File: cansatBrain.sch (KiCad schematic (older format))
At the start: 33 parts

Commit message: everything
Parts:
- removed BT?: BATTERY, symbol BATTERY
- removed C? (x3): 10 uF, symbol C
- removed C?: 0.1 uF, symbol C
- removed D?: DIODE, symbol DIODE
- removed L?: 1.5 uH, symbol INDUCTOR
- removed Q?: MOS_P, symbol MOS_P
- removed R? (x4): R, symbol R
- removed SW?: SW_PUSH_4, symbol SW_PUSH_4
- removed U?: TMP102, symbol TMP102
- removed U?: TPS63031, symbol TPS63031
- added C? (x4): 100nF, symbol C
- added C? (x4): 10uF, symbol CP2
- added C? (x3): 1uF, symbol C
- added C?: 10nF, symbol C
- added C?: 0.1uF, symbol C
- added C?: 10uF, symbol C
- added P?: Ext_Temp, symbol CONN_01X04
- added SW?: SW_PUSH_4, symbol SW_PUSH_4
- R? (x5): value R -> 1K
- R? (x2): value R -> 1M
- R? (x2): value R -> 100
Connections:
- net labels added: BAT_SENSE, BUTTON, GNDA, MPU_INT, SD_CS, VCCA, XBEE_SLEEP, XTRA_RX, XTRA_TX
- net labels removed: VBAT, VIN
- wire segments 115 -> 116
- no-connect marks 1 -> 31
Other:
- note removed: "1/3N lithium cell"
- moved on the sheet: P?, Q?, R?, U?

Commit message: ran rescue
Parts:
- C? (x10): symbol C -> C-RESCUE-cansatBrain
- R? (x9): symbol R -> R-RESCUE-cansatBrain
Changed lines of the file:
@@
 EESchema Schematic File Version 2
+LIBS:cansatBrain-rescue
 LIBS:power
 LIBS:device
@@
 $EndDescr
 $Comp
-L GND #PWR?
+L GND-RESCUE-cansatBrain #PWR?
 U 1 1 55860B07
 P 850 7500
@@
 SCL
 $Comp
-L R R?
+L R-RESCUE-cansatBrain R?
 U 1 1 5593D5CF
 P 2800 4450
@@
 $EndComp
 $Comp
-L R R?
+L R-RESCUE-cansatBrain R?
 U 1 1 5593D624
 P 2800 4650
@@
 XBEE_TX
 $Comp
-L R R?
+L R-RESCUE-cansatBrain R?
 U 1 1 5593EE71
 P 2750 4150
@@
 $EndComp
 $Comp
-L R R?
+L R-RESCUE-cansatBrain R?
 U 1 1 5593EE77
 P 3100 4250
@@
 	7950 3450 7950 3350
 $Comp
-L GND #PWR?
+L GND-RESCUE-cansatBrain #PWR?
 U 1 1 55947E65
 P 7550 3450
@@
 	7550 3350 7950 3350
 $Comp
-L GND #PWR?
+L GND-RESCUE-cansatBrain #PWR?
 U 1 1 55948C97
 P 5350 7300
@@
 	2450 1200 2450 1250
 $Comp
-L GND #PWR?
+L GND-RESCUE-cansatBrain #PWR?
 U 1 1 5594DF95
 P 2450 1250
@@
 	2300 1100 2900 1100
 $Comp
-L R R?
+L R-RESCUE-cansatBrain R?
 U 1 1 55950062
 P 2350 1650
@@
 $EndComp
 $Comp
-L R R?
+L R-RESCUE-cansatBrain R?
 U 1 1 55951A1D
 P 2650 1000
@@
 Connection ~ 2100 1550
 $Comp
-L R R?
+L R-RESCUE-cansatBrain R?
 U 1 1 5595265B
 P 1650 1550
@@
 Connection ~ 7500 950
 $Comp
-L GND #PWR?
+L GND-RESCUE-cansatBrain #PWR?
 U 1 1 5595A08F
 P 7500 1250
@@
 $EndComp
 $Comp
-L R R?
+L R-RESCUE-cansatBrain R?
 U 1 1 55962027
 P 4550 6050
@@
 SCL
 $Comp
-L R R?
+L R-RESCUE-cansatBrain R?
 U 1 1 55967163
 P 4800 5750
@@
 $EndComp
 $Comp
-L GNDA #PWR?
+L GNDA-RESCUE-cansatBrain #PWR?
 U 1 1 55947C02
 P 5150 3950
@@
 $EndComp
 $Comp
-L GNDA #PWR?
+L GNDA-RESCUE-cansatBrain #PWR?
 U 1 1 5594830F
 P 6000 2200
@@
 $EndSheet
 $Comp
-L C C?
+L C-RESCUE-cansatBrain C?
 U 1 1 5595C2F2
 P 6150 3300
@@
 $EndComp
 $Comp
-L C C?
+L C-RESCUE-cansatBrain C?
 U 1 1 5595C2FE
 P 6400 3300
@@
 $EndComp
 $Comp
-L GNDA #PWR?
+L GNDA-RESCUE-cansatBrain #PWR?
 U 1 1 5595C306
 P 6650 3500
@@
 $EndComp
 $Comp
-L GNDA #PWR?
+L GNDA-RESCUE-cansatBrain #PWR?
 U 1 1 5595C30C
 P 6400 3500
@@
 $EndComp
 $Comp
-L GNDA #PWR?
+L GNDA-RESCUE-cansatBrain #PWR?
 U 1 1 5595C312
 P 6150 3500
@@
 Connection ~ 6150 3050
 $Comp
-L C C?
+L C-RESCUE-cansatBrain C?
 U 1 1 5595DCAA
 P 5850 3800
@@
 	5850 3600 5600 3600
 $Comp
-L GNDA #PWR?
+L GNDA-RESCUE-cansatBrain #PWR?
 U 1 1 5595E48A
 P 5850 4050
@@
 $EndComp
 $Comp
-L GNDA #PWR?
+L GNDA-RESCUE-cansatBrain #PWR?
 U 1 1 5594C5A2
 P 4450 5000
@@
 BAT_SENSE
 $Comp
-L GNDA #PWR?
+L GNDA-RESCUE-cansatBrain #PWR?
 U 1 1 5595C817
 P 4600 1550
@@
 	5350 6300 6100 6300
 $Comp
-L C C?
+L C-RESCUE-cansatBrain C?
 U 1 1 559679F4
 P 5600 6550
@@
 $EndComp
 $Comp
-L C C?
+L C-RESCUE-cansatBrain C?
 U 1 1 55967A00
 P 5850 6550
@@
 Connection ~ 5350 6300
 $Comp
-L GND #PWR?
+L GND-RESCUE-cansatBrain #PWR?
 U 1 1 55967EFF
 P 5600 6750
@@
 $EndComp
 $Comp
-L GND #PWR?
+L GND-RESCUE-cansatBrain #PWR?
 U 1 1 55967F36
 P 5850 6750
@@
 $EndComp
 $Comp
-L GND #PWR?
+L GND-RESCUE-cansatBrain #PWR?
 U 1 1 55967F6D
 P 6100 6750
@@
 $EndComp
 $Comp
-L C C?
+L C-RESCUE-cansatBrain C?
 U 1 1 5596DE7F
 P 4650 2400
@@
 $EndComp
 $Comp
-L GNDA #PWR?
+L GNDA-RESCUE-cansatBrain #PWR?
 U 1 1 5596E206
 P 4650 2600
@@
 	3600 1800 3600 1900
 $Comp
-L C C?
+L C-RESCUE-cansatBrain C?
 U 1 1 5596F8E8
 P 3600 2100
@@
 $EndComp
 $Comp
-L GNDA #PWR?
+L GNDA-RESCUE-cansatBrain #PWR?
 U 1 1 5596F93A
 P 3600 2300
@@
 NoConn ~ 5950 1800
 $Comp
-L GNDA #PWR?
+L GNDA-RESCUE-cansatBrain #PWR?
 U 1 1 5597096F
 P 6000 1950
@@
 NoConn ~ 5950 1400
 $Comp
-L GNDA #PWR?
+L GNDA-RESCUE-cansatBrain #PWR?
 U 1 1 55970FAD
 P 4300 1150
@@
 	4300 1100 4750 1100
 $Comp
-L C C?
+L C-RESCUE-cansatBrain C?
 U 1 1 5597608A
 P 3850 2350
@@
 $EndComp
 $Comp
-L C C?
+L C-RESCUE-cansatBrain C?
 U 1 1 55976096
 P 4100 2350
@@
 $EndComp
 $Comp
-L GNDA #PWR?
+L GNDA-RESCUE-cansatBrain #PWR?
 U 1 1 5597609C
 P 4350 2550
@@
 $EndComp
 $Comp
-L GNDA #PWR?
+L GNDA-RESCUE-cansatBrain #PWR?
 U 1 1 559760A2
 P 4100 2550
@@
 $EndComp
 $Comp
-L GNDA #PWR?
+L GNDA-RESCUE-cansatBrain #PWR?
 U 1 1 559760A8
 P 3850 2550
@@
 NoConn ~ 7700 1400
 $Comp
-L C C?
+L C-RESCUE-cansatBrain C?
 U 1 1 5598A4C3
 P 700 4250
@@
 $EndComp
 $Comp
-L GND #PWR?
+L GND-RESCUE-cansatBrain #PWR?
 U 1 1 5598A51D
 P 700 4450
@@
 Connection ~ 900  4050
 $Comp
-L GND #PWR?
+L GND-RESCUE-cansatBrain #PWR?
 U 1 1 5598DC65
 P 6850 1350
@@
 	7450 4600 7450 4750
 $Comp
-L GND #PWR?
+L GND-RESCUE-cansatBrain #PWR?
 U 1 1 559A8264
 P 7450 4750

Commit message: worked on stuff
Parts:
- P?: value Ext_Temp -> I2C

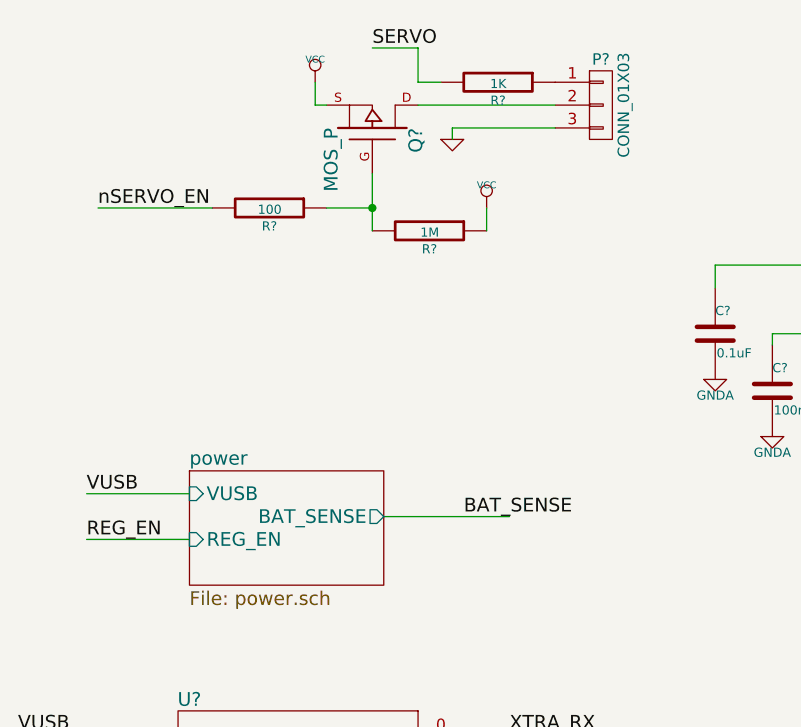
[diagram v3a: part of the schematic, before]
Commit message: changed button voltage clamp
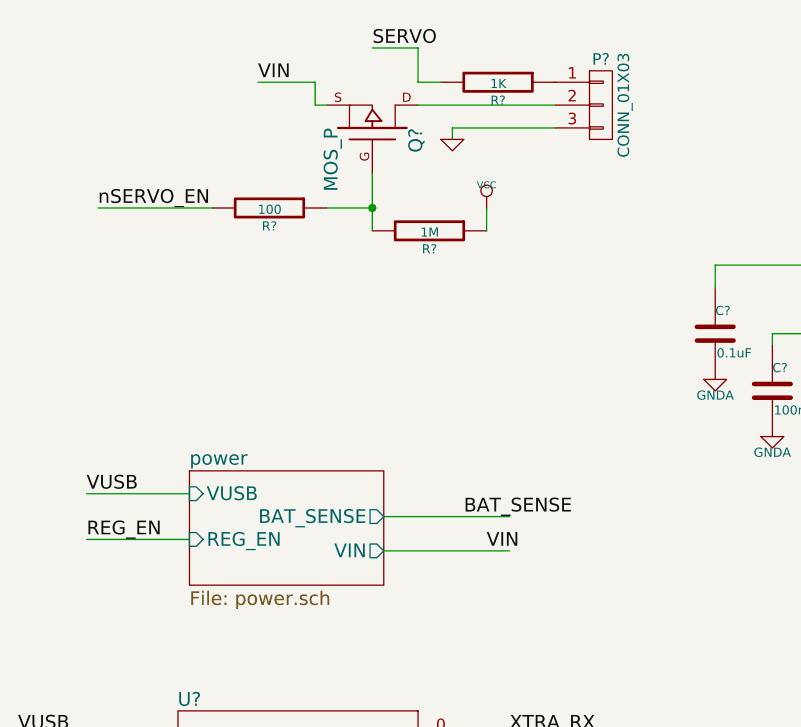
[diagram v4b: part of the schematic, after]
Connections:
- net labels added: VIN
- wire segments 116 -> 118
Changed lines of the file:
@@
-	1    0    0    -1
-$EndComp
-$Comp
-L VCC #PWR06
-U 1 1 5594DE9A
-P 1850 1000
-F 0 "#PWR06" H 1850 1100 30  0001 C CNN
-F 1 "VCC" H 1850 1100 30  0000 C CNN
-F 2 "" H 1850 1000 60  0000 C CNN
-F 3 "" H 1850 1000 60  0000 C CNN
-	1    1850 1000
 	1    0    0    -1
 $EndComp
@@
 F3 "REG_EN" I L 1300 3000 60
 F4 "BAT_SENSE" O R 2150 2900 60
+F5 "VIN" O R 2150 3050 60
 $EndSheet
 $Comp
@@
 NoConn ~ 2500 5350
 NoConn ~ 2500 5450
+Wire Wire Line
+	2150 3050 2700 3050
+Text Label 2600 3050 0    60   ~ 0
+VIN
+Wire Wire Line
+	1850 1000 1600 1000
+Text Label 1600 1000 0    60   ~ 0
+VIN
 $EndSCHEMATC

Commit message: did more work
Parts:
- removed SW?: SW_PUSH_4, symbol SW_PUSH_4
- added P?: CONN_01X03, symbol CONN_01X03
- added Q?: MOS_P, symbol MOS_P
- added R?: 1M, symbol R-RESCUE-cansatBrain
- added R?: 100, symbol R-RESCUE-cansatBrain
- added R? (x2): 10k, symbol R
- added U?: ArduCAM-M-2MP, symbol ArduCAM-M-2MP
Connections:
- net labels added: +5V, CAM_CS, PITOT_TUBE, nPITOT_EN
- wire segments 118 -> 140
- no-connect marks 31 -> 28

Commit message: more stuff
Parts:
- added P4: CONN_01X04, symbol CONN_01X04
- gave numbers to parts that had none: 40
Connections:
- net M0SI is gone; now on net MOSI: U1.11 (11(DOUT))
- net GND: now also P4.4 (P4)
- net VCC: now also P4.3 (P3)
- net VCCA: now also C6.1
- net XTRA_RX: now also P4.2 (P2)
- net XTRA_TX: now also P4.1 (P1)

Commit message: footprints
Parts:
- C1, C10, C11, C12, C13, C14, C2, C3, C4, C5, C6, C7, C8, C9: footprint (none) -> Capacitors_SMD:C_0402
- P1, P3: footprint (none) -> Pin_Headers:Pin_Header_Straight_1x03
- P2, P4: footprint (none) -> Pin_Headers:Pin_Header_Straight_1x04
- Q1, Q2, Q3: footprint (none) -> TO_SOT_Packages_SMD:SOT-23_Handsoldering
- R1, R10, R11, R12, R13, R2, R3, R4, R5, R6, R7, R8, R9: footprint (none) -> Resistors_SMD:R_0402
- U1: footprint (none) -> Housings_DIP:DIP-28_W15.24mm
- U2: footprint (none) -> SMD_Packages:SOIC-8-N
- U3: footprint (none) -> Pin_Headers:Pin_Header_Straight_1x06
- U4: footprint (none) -> Housings_DFN_QFN:QFN-24-1EP_3x3mm_Pitch0.4mm
- U5: footprint (none) -> Pin_Headers:Pin_Header_Straight_1x05
- U6: footprint (none) -> Housings_DIP:DIP-20_W7.62mm_LongPads
- U7: footprint (none) -> Pin_Headers:Pin_Header_Straight_1x08
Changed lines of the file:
@@
 F 0 "U4" H 5350 2350 60  0000 C CNN
 F 1 "MPU-9250" H 5350 950 60  0000 C CNN
-F 2 "" H 5450 1750 60  0000 C CNN
+F 2 "Housings_DFN_QFN:QFN-24-1EP_3x3mm_Pitch0.4mm" H 5450 1750 60  0001 C CNN
 F 3 "" H 5450 1750 60  0000 C CNN
 	1    5350 1650
@@
 F 0 "U6" H 7950 2400 60  0000 C CNN
 F 1 "XBee" H 8000 800 60  0000 C CNN
-F 2 "" H 9350 1050 60  0000 C CNN
+F 2 "Housings_DIP:DIP-20_W7.62mm_LongPads" H 9350 1050 60  0001 C CNN
 F 3 "" H 9350 1050 60  0000 C CNN
 	1    8650 1600
@@
 F 0 "U2" H 4800 3100 60  0000 L CNN
 F 1 "MPL3115A2" H 5200 3100 60  0000 L CNN
-F 2 "" H 6400 1700 60  0000 C CNN
+F 2 "SMD_Packages:SOIC-8-N" H 6400 1700 60  0001 C CNN
 F 3 "" H 6400 1700 60  0000 C CNN
 	1    5150 3450
@@
 F 0 "U3" H 5000 7100 60  0000 C CNN
 F 1 "microSD" H 5050 6500 60  0000 C CNN
-F 2 "" H 4950 6750 60  0000 C CNN
+F 2 "Pin_Headers:Pin_Header_Straight_1x06" H 4950 6750 60  0001 C CNN
 F 3 "" H 4950 6750 60  0000 C CNN
 	1    5250 6800
@@
 F 0 "U5" H 8200 3900 60  0000 C CNN
 F 1 "LS20031" H 8350 3100 60  0000 C CNN
-F 2 "" H 7900 3550 60  0000 C CNN
+F 2 "Pin_Headers:Pin_Header_Straight_1x05" H 7900 3550 60  0001 C CNN
 F 3 "" H 7900 3550 60  0000 C CNN
 	1    8250 3500
@@
 F 0 "U1" H 1300 6900 60  0000 C CNN
 F 1 "Teensy_LC" H 1450 3050 60  0000 C CNN
-F 2 "" H 1650 5900 60  0000 C CNN
+F 2 "Housings_DIP:DIP-28_W15.24mm" H 1650 5900 60  0001 C CNN
 F 3 "" H 1650 5900 60  0000 C CNN
 	1    1800 5300
@@
 F 0 "R5" V 2880 4450 40  0000 C CNN
 F 1 "1K" V 2807 4451 40  0000 C CNN
-F 2 "" V 2730 4450 30  0000 C CNN
+F 2 "Resistors_SMD:R_0402" V 2730 4450 30  0001 C CNN
 F 3 "" H 2800 4450 30  0000 C CNN
 	1    2800 4450
@@
 F 0 "R6" V 2880 4650 40  0000 C CNN
 F 1 "1K" V 2807 4651 40  0000 C CNN
-F 2 "" V 2730 4650 30  0000 C CNN
+F 2 "Resistors_SMD:R_0402" V 2730 4650 30  0001 C CNN
 F 3 "" H 2800 4650 30  0000 C CNN
 	1    2800 4650
@@
 F 0 "R4" V 2830 4150 40  0000 C CNN
 F 1 "1K" V 2757 4151 40  0000 C CNN
-F 2 "" V 2680 4150 30  0000 C CNN
+F 2 "Resistors_SMD:R_0402" V 2680 4150 30  0001 C CNN
 F 3 "" H 2750 4150 30  0000 C CNN
 	1    2750 4150
@@
 F 0 "R7" V 3180 4250 40  0000 C CNN
 F 1 "1K" V 3107 4251 40  0000 C CNN
-F 2 "" V 3030 4250 30  0000 C CNN
+F 2 "Resistors_SMD:R_0402" V 3030 4250 30  0001 C CNN
 F 3 "" H 3100 4250 30  0000 C CNN
 	1    3100 4250
@@
 F 0 "P1" H 3100 1300 50  0000 C CNN
 F 1 "CONN_01X03" V 3200 1100 50  0000 C CNN
-F 2 "" H 3100 1100 60  0000 C CNN
+F 2 "Pin_Headers:Pin_Header_Straight_1x03" H 3100 1100 60  0001 C CNN
 F 3 "" H 3100 1100 60  0000 C CNN
 	1    3100 1100
@@
 F 0 "Q1" H 2100 1390 60  0000 R CNN
 F 1 "MOS_P" H 2100 1020 60  0000 R CNN
-F 2 "" H 2100 1200 60  0000 C CNN
+F 2 "TO_SOT_Packages_SMD:SOT-23_Handsoldering" H 2100 1200 60  0001 C CNN
 F 3 "" H 2100 1200 60  0000 C CNN
 	1    2100 1200
@@
 F 0 "R2" V 2430 1650 40  0000 C CNN
 F 1 "1M" V 2357 1651 40  0000 C CNN
-F 2 "" V 2280 1650 30  0000 C CNN
+F 2 "Resistors_SMD:R_0402" V 2280 1650 30  0001 C CNN
 F 3 "" H 2350 1650 30  0000 C CNN
 	1    2350 1650
@@
 F 0 "R3" V 2730 1000 40  0000 C CNN
 F 1 "1K" V 2657 1001 40  0000 C CNN
-F 2 "" V 2580 1000 30  0000 C CNN
+F 2 "Resistors_SMD:R_0402" V 2580 1000 30  0001 C CNN
 F 3 "" H 2650 1000 30  0000 C CNN
 	1    2650 1000
@@
 F 0 "R1" V 1730 1550 40  0000 C CNN
 F 1 "100" V 1657 1551 40  0000 C CNN
-F 2 "" V 1580 1550 30  0000 C CNN
+F 2 "Resistors_SMD:R_0402" V 1580 1550 30  0001 C CNN
 F 3 "" H 1650 1550 30  0000 C CNN
 	1    1650 1550
@@
 F 0 "Q2" H 5250 6240 60  0000 R CNN
 F 1 "MOS_P" H 5250 5870 60  0000 R CNN
-F 2 "" H 5250 6050 60  0000 C CNN
+F 2 "TO_SOT_Packages_SMD:SOT-23_Handsoldering" H 5250 6050 60  0001 C CNN
 F 3 "" H 5250 6050 60  0000 C CNN
 	1    5250 6050
@@
 F 0 "R8" V 4630 6050 40  0000 C CNN
 F 1 "100" V 4557 6051 40  0000 C CNN
-F 2 "" V 4480 6050 30  0000 C CNN
+F 2 "Resistors_SMD:R_0402" V 4480 6050 30  0001 C CNN
 F 3 "" H 4550 6050 30  0000 C CNN
 	1    4550 6050
@@
 F 0 "R9" V 4880 5750 40  0000 C CNN
 F 1 "1M" V 4807 5751 40  0000 C CNN
-F 2 "" V 4730 5750 30  0000 C CNN
+F 2 "Resistors_SMD:R_0402" V 4730 5750 30  0001 C CNN
 F 3 "" H 4800 5750 30  0000 C CNN
 	1    4800 5750
@@
 F 0 "C11" H 6150 3400 40  0000 L CNN
 F 1 "100nF" H 6156 3215 40  0000 L CNN
-F 2 "" H 6188 3150 30  0000 C CNN
+F 2 "Capacitors_SMD:C_0402" H 6188 3150 30  0001 C CNN
 F 3 "" H 6150 3300 60  0000 C CNN
 	1    6150 3300
@@
 F 0 "C13" H 6650 3400 40  0000 L CNN
 F 1 "10uF" H 6656 3215 40  0000 L CNN
-F 2 "" H 6688 3150 30  0000 C CNN
+F 2 "Capacitors_SMD:C_0402" H 6688 3150 30  0001 C CNN
 F 3 "" H 6650 3300 60  0000 C CNN
 	1    6650 3300
@@
 F 0 "C12" H 6400 3400 40  0000 L CNN
 F 1 "1uF" H 6406 3215 40  0000 L CNN
-F 2 "" H 6438 3150 30  0000 C CNN
+F 2 "Capacitors_SMD:C_0402" H 6438 3150 30  0001 C CNN
 F 3 "" H 6400 3300 60  0000 C CNN
 	1    6400 3300
@@
 F 0 "C8" H 5850 3900 40  0000 L CNN
 F 1 "100nF" H 5856 3715 40  0000 L CNN
-F 2 "" H 5888 3650 30  0000 C CNN
+F 2 "Capacitors_SMD:C_0402" H 5888 3650 30  0001 C CNN
 F 3 "" H 5850 3800 60  0000 C CNN
 	1    5850 3800
@@
 F 0 "P2" H 5500 5200 50  0000 C CNN
 F 1 "I2C" V 5600 4950 50  0000 C CNN
-F 2 "" H 5500 4950 60  0000 C CNN
+F 2 "Pin_Headers:Pin_Header_Straight_1x04" H 5500 4950 60  0001 C CNN
 F 3 "" H 5500 4950 60  0000 C CNN
 	1    5500 4950
@@
 F 0 "C7" H 5600 6650 40  0000 L CNN
 F 1 "100nF" H 5606 6465 40  0000 L CNN
-F 2 "" H 5638 6400 30  0000 C CNN
+F 2 "Capacitors_SMD:C_0402" H 5638 6400 30  0001 C CNN
 F 3 "" H 5600 6550 60  0000 C CNN
 	1    5600 6550
@@
 F 0 "C10" H 6100 6650 40  0000 L CNN
 F 1 "10uF" H 6106 6465 40  0000 L CNN
-F 2 "" H 6138 6400 30  0000 C CNN
+F 2 "Capacitors_SMD:C_0402" H 6138 6400 30  0001 C CNN
 F 3 "" H 6100 6550 60  0000 C CNN
 	1    6100 6550
@@
 F 0 "C9" H 5850 6650 40  0000 L CNN
 F 1 "1uF" H 5856 6465 40  0000 L CNN
-F 2 "" H 5888 6400 30  0000 C CNN
+F 2 "Capacitors_SMD:C_0402" H 5888 6400 30  0001 C CNN
 F 3 "" H 5850 6550 60  0000 C CNN
 	1    5850 6550
@@
 F 0 "C6" H 4650 2500 40  0000 L CNN
 F 1 "10nF" H 4656 2315 40  0000 L CNN
-F 2 "" H 4688 2250 30  0000 C CNN
+F 2 "Capacitors_SMD:C_0402" H 4688 2250 30  0001 C CNN
 F 3 "" H 4650 2400 60  0000 C CNN
 	1    4650 2400
@@
 F 0 "C2" H 3600 2200 40  0000 L CNN
 F 1 "0.1uF" H 3606 2015 40  0000 L CNN
-F 2 "" H 3638 1950 30  0000 C CNN
+F 2 "Capacitors_SMD:C_0402" H 3638 1950 30  0001 C CNN
 F 3 "" H 3600 2100 60  0000 C CNN
 	1    3600 2100
@@
 F 0 "C3" H 3850 2450 40  0000 L CNN
 F 1 "100nF" H 3856 2265 40  0000 L CNN
-F 2 "" H 3888 2200 30  0000 C CNN
+F 2 "Capacitors_SMD:C_0402" H 3888 2200 30  0001 C CNN
 F 3 "" H 3850 2350 60  0000 C CNN
 	1    3850 2350
@@
 F 0 "C5" H 4350 2450 40  0000 L CNN
 F 1 "10uF" H 4356 2265 40  0000 L CNN
-F 2 "" H 4388 2200 30  0000 C CNN
+F 2 "Capacitors_SMD:C_0402" H 4388 2200 30  0001 C CNN
 F 3 "" H 4350 2350 60  0000 C CNN
 	1    4350 2350
@@
 F 0 "C4" H 4100 2450 40  0000 L CNN
 F 1 "1uF" H 4106 2265 40  0000 L CNN
-F 2 "" H 4138 2200 30  0000 C CNN
+F 2 "Capacitors_SMD:C_0402" H 4138 2200 30  0001 C CNN
 F 3 "" H 4100 2350 60  0000 C CNN
 	1    4100 2350
@@
 F 0 "C1" H 700 4350 40  0000 L CNN
 F 1 "10uF" H 706 4165 40  0000 L CNN
-F 2 "" H 738 4100 30  0000 C CNN
+F 2 "Capacitors_SMD:C_0402" H 738 4100 30  0001 C CNN
 F 3 "" H 700 4250 60  0000 C CNN
 	1    700  4250
@@
 F 0 "C14" H 6850 1250 40  0000 L CNN
 F 1 "10uF" H 6856 1065 40  0000 L CNN
-F 2 "" H 6888 1000 30  0000 C CNN
+F 2 "Capacitors_SMD:C_0402" H 6888 1000 30  0001 C CNN
 F 3 "" H 6850 1150 60  0000 C CNN
 	1    6850 1150
@@
 F 0 "U7" H 9500 4300 60  0000 C CNN
 F 1 "ArduCAM-M-2MP" H 9850 4200 60  0000 C CNN
-F 2 "" H 9600 3500 60  0000 C CNN
+F 2 "Pin_Headers:Pin_Header_Straight_1x08" H 9600 3500 60  0001 C CNN
 F 3 "" H 9600 3500 60  0000 C CNN
 	1    9650 3650
@@
 F 0 "P3" H 9300 6250 50  0000 C CNN
 F 1 "CONN_01X03" V 9400 6050 50  0000 C CNN
-F 2 "" H 9300 6050 50  0000 C CNN
+F 2 "Pin_Headers:Pin_Header_Straight_1x03" H 9300 6050 50  0001 C CNN
 F 3 "" H 9300 6050 50  0000 C CNN
 	1    9300 6050
@@
 F 0 "Q3" H 8300 6340 60  0000 R CNN
 F 1 "MOS_P" H 8300 5970 60  0000 R CNN
-F 2 "" H 8300 6150 60  0000 C CNN
+F 2 "TO_SOT_Packages_SMD:SOT-23_Handsoldering" H 8300 6150 60  0001 C CNN
 F 3 "" H 8300 6150 60  0000 C CNN
 	1    8300 6150
@@
 F 0 "R11" V 8630 6600 40  0000 C CNN
 F 1 "1M" V 8557 6601 40  0000 C CNN
-F 2 "" V 8480 6600 30  0000 C CNN
+F 2 "Resistors_SMD:R_0402" V 8480 6600 30  0001 C CNN
 F 3 "" H 8550 6600 30  0000 C CNN
 	1    8550 6600
@@
 F 0 "R10" V 7930 6500 40  0000 C CNN
 F 1 "100" V 7857 6501 40  0000 C CNN
-F 2 "" V 7780 6500 30  0000 C CNN
+F 2 "Resistors_SMD:R_0402" V 7780 6500 30  0001 C CNN
 F 3 "" H 7850 6500 30  0000 C CNN
 	1    7850 6500
@@
 F 0 "R12" V 9830 5800 50  0000 C CNN
 F 1 "10k" V 9750 5800 50  0000 C CNN
-F 2 "" V 9680 5800 50  0000 C CNN
+F 2 "Resistors_SMD:R_0402" V 9680 5800 50  0001 C CNN
 F 3 "" H 9750 5800 50  0000 C CNN
 	1    9750 5800
@@
 F 0 "R13" V 9830 6100 50  0000 C CNN
 F 1 "10k" V 9750 6100 50  0000 C CNN
-F 2 "" V 9680 6100 50  0000 C CNN
+F 2 "Resistors_SMD:R_0402" V 9680 6100 50  0001 C CNN
 F 3 "" H 9750 6100 50  0000 C CNN
 	1    9750 6100
@@
 F 0 "P4" H 7100 5200 50  0000 C CNN
 F 1 "CONN_01X04" V 7200 4950 50  0000 C CNN
-F 2 "" H 7100 4950 50  0000 C CNN
+F 2 "Pin_Headers:Pin_Header_Straight_1x04" H 7100 4950 50  0001 C CNN
 F 3 "" H 7100 4950 50  0000 C CNN
 	1    7100 4950

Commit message: more stuff
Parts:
- P1: value CONN_01X03 -> SERVO
- P3: value CONN_01X03 -> PITOT
- P4: value CONN_01X04 -> SERIAL
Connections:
- net VCC: no longer R2.1
- net VIN: now also R2.1
